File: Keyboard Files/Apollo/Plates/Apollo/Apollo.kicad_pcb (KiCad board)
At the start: 2 copper layers, 166.1 x 133.7 mm, 37 parts

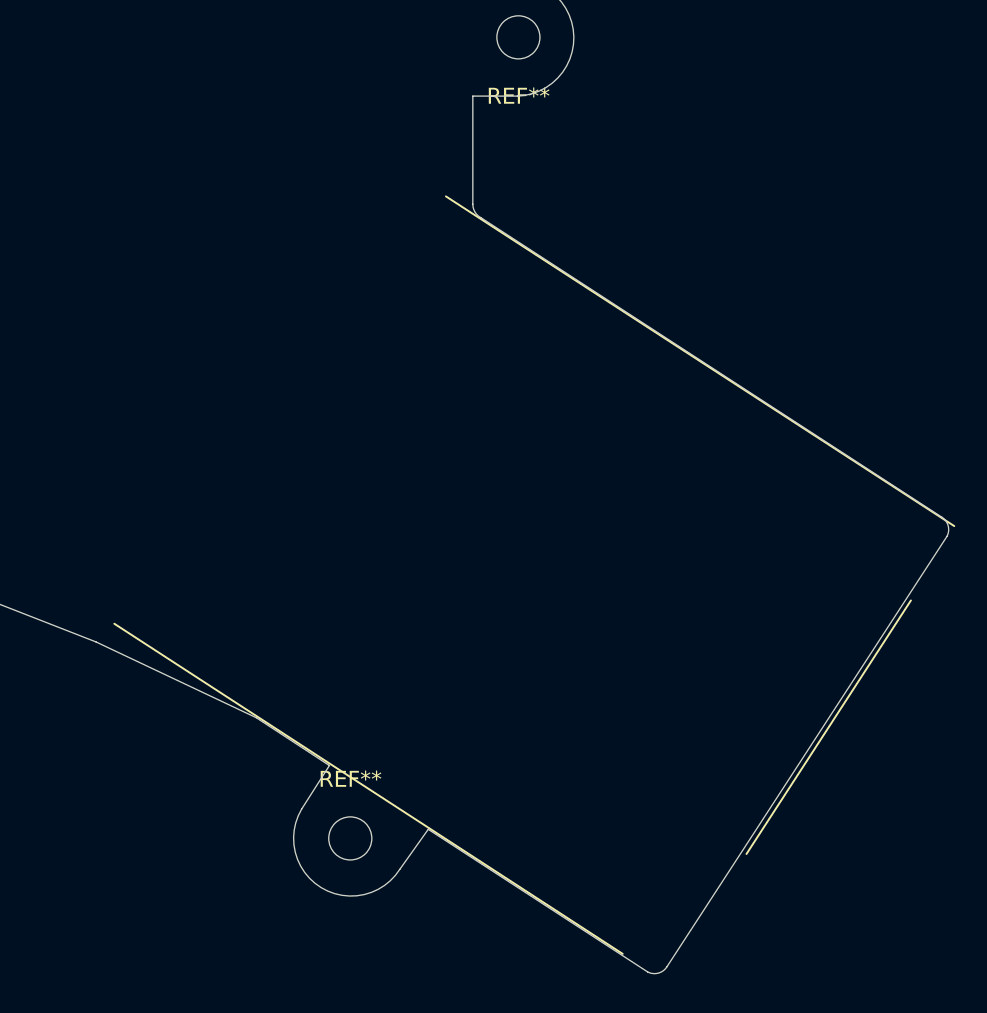
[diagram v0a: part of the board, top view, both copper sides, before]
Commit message: Redo thumb keys plates
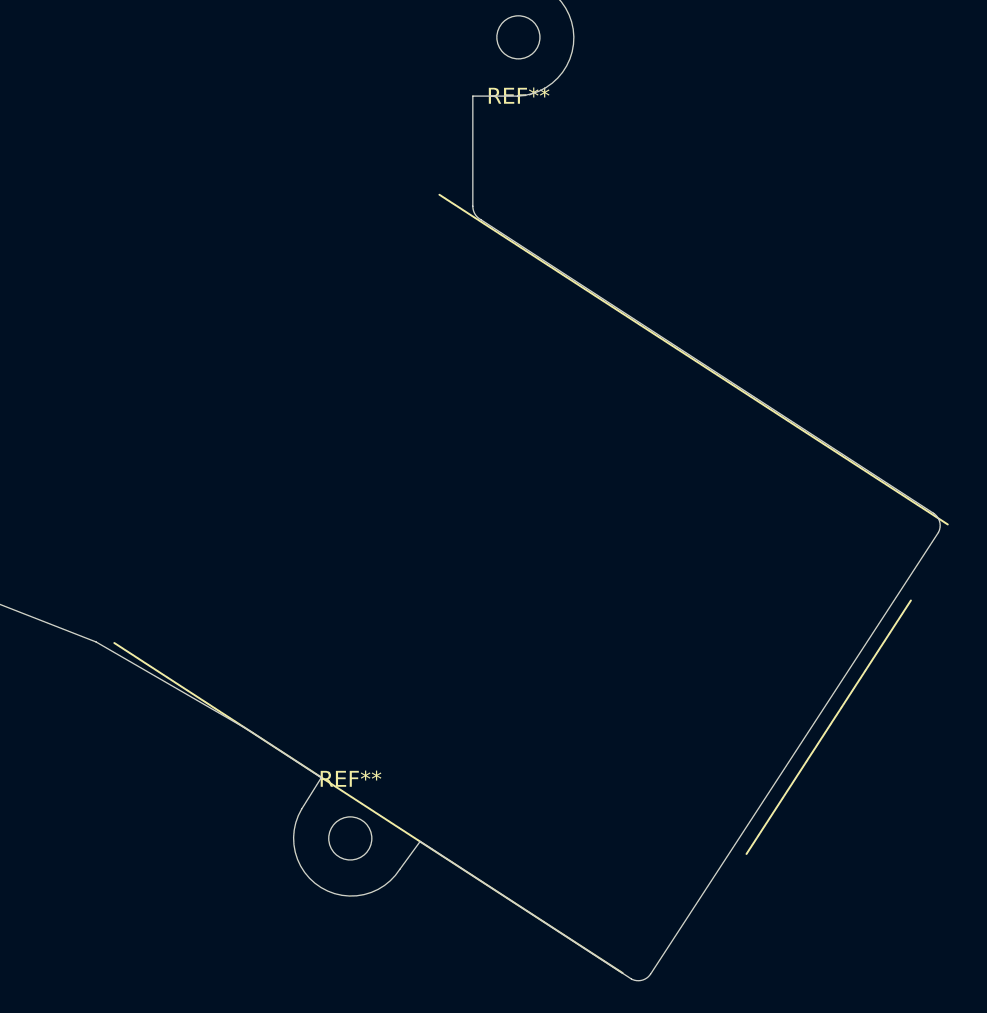
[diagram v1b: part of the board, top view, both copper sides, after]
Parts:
- turned REF** to 57 degrees (x2)
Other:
- board size 166.1 x 133.7 mm -> 165.6 x 134.1 mm
